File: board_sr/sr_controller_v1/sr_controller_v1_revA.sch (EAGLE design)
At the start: 122 parts, among them IC2 74HC595D, J2 WIRE_HOLE-14AWG, J3 WIRE_HOLE-14AWG, J4 WIRE_HOLE-14AWG, J5 WIRE_HOLE-14AWG, J6 WIRE_HOLE-14AWG, J7 WIRE_HOLE-14AWG, J8 WIRE_HOLE-14AWG, J9 WIRE_HOLE-14AWG, K1 G5L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

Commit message: Add Casing CAD Drawing
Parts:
- added DUMMY_A, DUMMY_B, DUMMY_C: (no value), con-ptr500:AK500/2
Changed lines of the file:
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@@
 <setting verticaltext="up"/>
 </settings>
-<grid distance="0.1" unitdist="inch" unit="inch" style="lines" multiple="1" display="no" altdistance="0.01" altunitdist="inch" altunit="inch"/>
+<grid distance="0.05" unitdist="inch" unit="inch" style="lines" multiple="1" display="no" altdistance="0.01" altunitdist="inch" altunit="inch"/>
 <layers>
 <layer number="1" name="Top" color="4" fill="1" visible="no" active="no"/>
@@
 <part name="J8" library="powercube" deviceset="WIRE_HOLE-14AWG" device=""/>
 <part name="J9" library="powercube" deviceset="WIRE_HOLE-14AWG" device=""/>
+<part name="DUMMY_A" library="con-ptr500" deviceset="AK500/2" device=""/>
+<part name="DUMMY_B" library="con-ptr500" deviceset="AK500/2" device=""/>
+<part name="DUMMY_C" library="con-ptr500" deviceset="AK500/2" device=""/>
 </parts>
 <sheets>
@@
 <instance part="J8" gate="G$1" x="406.4" y="119.38"/>
 <instance part="J9" gate="G$1" x="406.4" y="109.22"/>
+<instance part="DUMMY_A" gate="-1" x="335.28" y="-25.4"/>
+<instance part="DUMMY_A" gate="-2" x="335.28" y="-29.21"/>
+<instance part="DUMMY_B" gate="-1" x="335.28" y="-33.02"/>
+<instance part="DUMMY_B" gate="-2" x="335.28" y="-36.83"/>
+<instance part="DUMMY_C" gate="-1" x="335.28" y="-40.64"/>
+<instance part="DUMMY_C" gate="-2" x="335.28" y="-44.45"/>
 </instances>
 <busses>

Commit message: Initial commit of getSensorData
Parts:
- R11: value R2K -> R1K
- R15: value R2K -> R10K
- R17: value R5K -> R5.1K
- R29, R33: value R2K -> R5.1K
- R32: value R100K -> R270K
- R8: value R1K -> R220R
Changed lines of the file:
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@@
 <setting verticaltext="up"/>
 </settings>
-<grid distance="0.05" unitdist="inch" unit="inch" style="lines" multiple="1" display="no" altdistance="0.01" altunitdist="inch" altunit="inch"/>
+<grid distance="0.1" unitdist="inch" unit="inch" style="lines" multiple="1" display="no" altdistance="0.01" altunitdist="inch" altunit="inch"/>
 <layers>
 <layer number="1" name="Top" color="4" fill="1" visible="no" active="no"/>
@@
 <part name="R6" library="resistor" deviceset="R-EU_" device="R0805" value="R1K"/>
 <part name="R7" library="resistor" deviceset="R-EU_" device="R0805" value="R10K"/>
-<part name="R8" library="resistor" deviceset="R-EU_" device="R0805" value="R1K"/>
+<part name="R8" library="resistor" deviceset="R-EU_" device="R0805" value="R220R"/>
 <part name="GND18" library="supply1" deviceset="GND" device=""/>
 <part name="U$2" library="SparkFun-AnalogIC" deviceset="ACS712" device=""/>
@@
 <part name="AGND5" library="supply1" deviceset="AGND" device=""/>
 <part name="R10" library="resistor" deviceset="R-EU_" device="R0805" value="R10K"/>
-<part name="R11" library="resistor" deviceset="R-EU_" device="R0805" value="R2K"/>
+<part name="R11" library="resistor" deviceset="R-EU_" device="R0805" value="R1K"/>
 <part name="R12" library="resistor" deviceset="R-EU_" device="R0805" value="R10K"/>
 <part name="R13" library="resistor" deviceset="R-EU_" device="R0805" value="R1K"/>
 <part name="R14" library="resistor" deviceset="R-EU_" device="R0805" value="R10K"/>
-<part name="R15" library="resistor" deviceset="R-EU_" device="R0805" value="R2K"/>
+<part name="R15" library="resistor" deviceset="R-EU_" device="R0805" value="R10K"/>
 <part name="R16" library="resistor" deviceset="R-EU_" device="R0805" value="R10K"/>
-<part name="R17" library="resistor" deviceset="R-EU_" device="R0805" value="R5K"/>
+<part name="R17" library="resistor" deviceset="R-EU_" device="R0805" value="R5.1K"/>
 <part name="GND21" library="supply1" deviceset="GND" device=""/>
 <part name="IC1" library="microbuilder" deviceset="GSM_SIM900_LITERAL" device=""/>
@@
 <part name="P+9" library="supply1" deviceset="+5V" device=""/>
 <part name="R28" library="resistor" deviceset="R-EU_" device="R0805" value="R10K"/>
-<part name="R29" library="resistor" deviceset="R-EU_" device="R0805" value="R2K"/>
+<part name="R29" library="resistor" deviceset="R-EU_" device="R0805" value="R5.1K"/>
 <part name="R30" library="resistor" deviceset="R-EU_" device="R0805" value="R1K"/>
 <part name="R31" library="resistor" deviceset="R-EU_" device="R0805" value="R2K"/>
 <part name="GND46" library="supply1" deviceset="GND" device=""/>
 <part name="U$9" library="bontor" deviceset="TRANSFORMER" device=""/>
-<part name="R32" library="resistor" deviceset="R-EU_" device="0309/10" value="R100K"/>
-<part name="R33" library="resistor" deviceset="R-EU_" device="0309/10" value="R2K"/>
+<part name="R32" library="resistor" deviceset="R-EU_" device="0309/10" value="R270K"/>
+<part name="R33" library="resistor" deviceset="R-EU_" device="0309/10" value="R5.1K"/>
 <part name="C14" library="resistor" deviceset="C-EU" device="C0805K" value="C100N"/>
 <part name="AGND6" library="supply1" deviceset="AGND" device=""/>

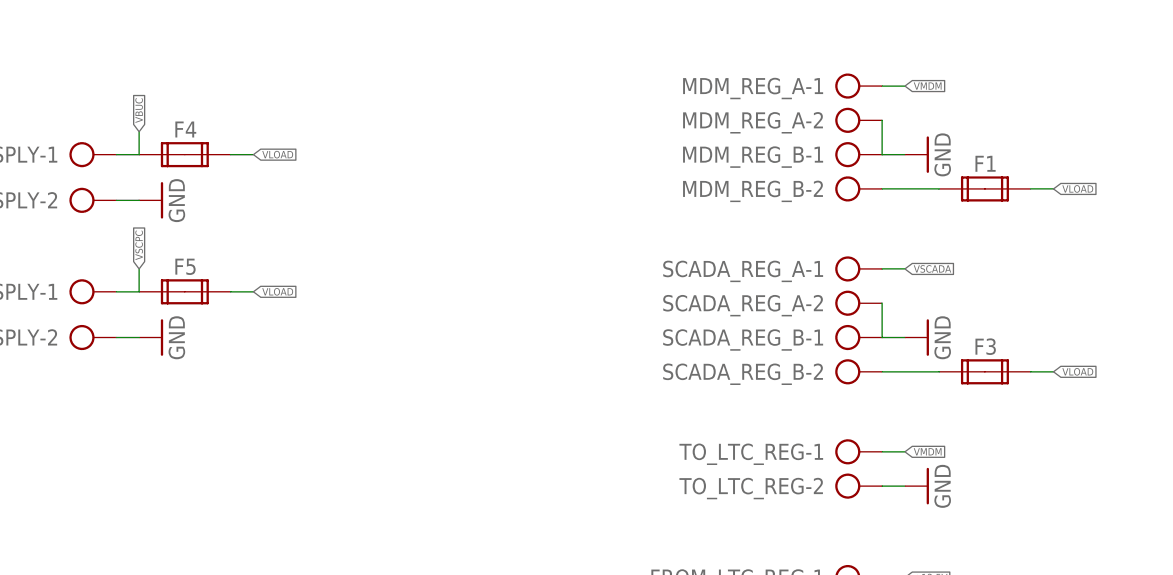
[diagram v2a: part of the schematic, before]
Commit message: Update sensor code to del data from DB after read
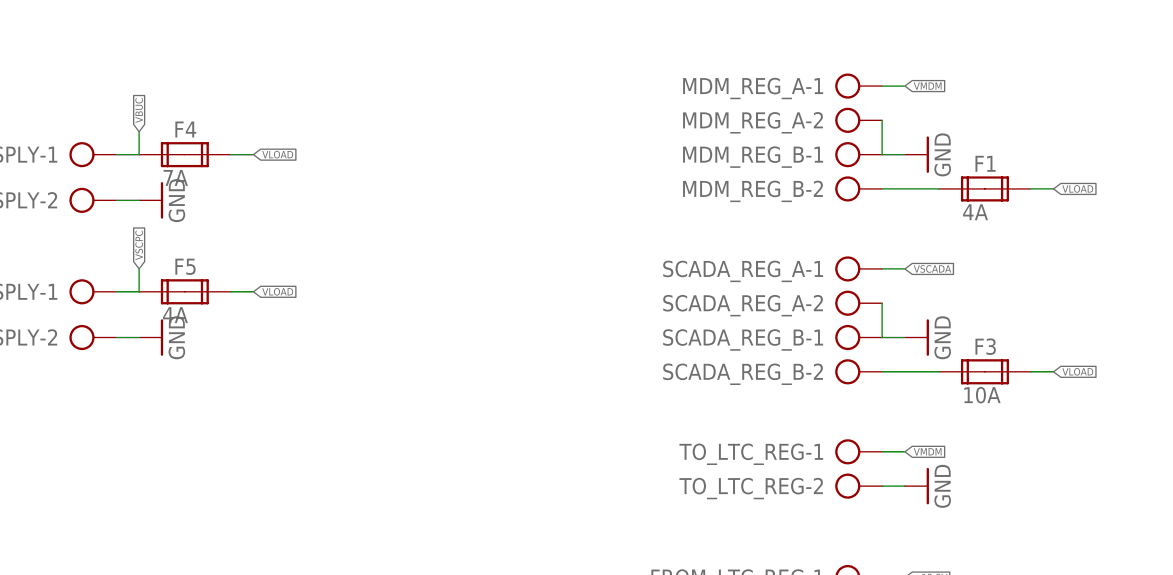
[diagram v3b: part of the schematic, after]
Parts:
- F1, F5: value (none) -> 4A
- F3: value (none) -> 10A
- F4: value (none) -> 7A
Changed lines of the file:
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@@
 <part name="SCADA_REG_A" library="con-ptr500" deviceset="AK300/2" device=""/>
 <part name="SCADA_REG_B" library="con-ptr500" deviceset="AK300/2" device=""/>
-<part name="F1" library="special" deviceset="FUSE2P" device=""/>
-<part name="F3" library="special" deviceset="FUSE2P" device=""/>
-<part name="F4" library="special" deviceset="FUSE2P" device=""/>
+<part name="F1" library="special" deviceset="FUSE2P" device="" value="4A"/>
+<part name="F3" library="special" deviceset="FUSE2P" device="" value="10A"/>
+<part name="F4" library="special" deviceset="FUSE2P" device="" value="7A"/>
 <part name="INDICATOR_CONN" library="con-lstb" deviceset="MA08-2" device=""/>
 <part name="GND2" library="supply1" deviceset="GND" device=""/>
@@
 <part name="GND52" library="supply1" deviceset="GND" device=""/>
 <part name="FROM_LTC_REG" library="con-ptr500" deviceset="AK300/3" device=""/>
-<part name="F5" library="special" deviceset="FUSE2P" device=""/>
+<part name="F5" library="special" deviceset="FUSE2P" device="" value="4A"/>
 <part name="MDM_SPLY_HT_X1_X3" library="con-ptr500" deviceset="AK300/5" device=""/>
 <part name="R5" library="resistor" deviceset="R-EU_" device="R0805" value="R1K"/>
